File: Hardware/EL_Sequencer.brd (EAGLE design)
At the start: 57.1 x 82.5 mm, 106 parts, among them J1 Battery, J2 DC-OUTPUT, J3 AC-INPUT, U1 LM317, U10 Z0103MN, U11 Z0103MN, U12 Z0103MN, U13 MOC3063S, U14 MOC3063S, U15 MOC3063S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

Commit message: Version 2.1 hardware files
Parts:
- added U$9: REVISION, SparkFun-Aesthetics:REVISION
- C1, C4, C5, C6, C7: device SparkFun:0402-CAP -> SparkFun-Capacitors:0603-CAP
- C2, C3: device SparkFun:EIA3216 -> SparkFun-Capacitors:EIA3216
- R1, R14, R15, R16, R17, R18, R19, R2, R20, R21, R26, R27, R28, R29, R30, R31, R32, R33: device SparkFun:0603-RES -> SparkFun-Resistors:0603-RES
- R10, R11, R12, R13, R22, R23, R24, R25, R3, R4, R5, R6, R7, R8, R9: device SparkFun:0402-RES -> SparkFun-Resistors:0603-RES
- moved FRAME1 19.1 mm to (5.08, -14.0)
- moved FRAME2 19.1 mm to (5.08, -14.0)
- moved R4 4.49 mm to (50.2, 4.45), turned to 180 degrees
- moved R6 3.18 mm to (20.3, 34.9), turned to 270 degrees
- moved R13 2.54 mm to (20.3, 38.1), turned to 270 degrees
- moved C5 1.91 mm to (17.8, 32.4), turned to 180 degrees
- moved R11 1.91 mm to (20.3, 20.3), turned to 270 degrees
- moved R5 1.91 mm to (21.6, 32.4), turned to 0 degrees
- moved C6 0.71 mm to (5.08, 17.5)
- moved C4 0.64 mm to (18.7, 17.4)
- moved R3 0.64 mm to (39.4, 4.45)
- turned R8 to 180 degrees
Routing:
- net GND: track 116.4 -> 122.3 mm
- net RXI: track 56.8 -> 61.1 mm
- net RST: track 40.7 -> 43.5 mm
- net FTDI_DTR: track 42.1 -> 39.6 mm
- net DTR: track 12.7 -> 14.9 mm
- net VCC: track 154.0 -> 156.1 mm
- net ADC_7*: track 6.95 -> 8.51 mm
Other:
- board text added: "Nathan Seidle, Mike Grusin"
- board text added: "Toni Klopfenstein"

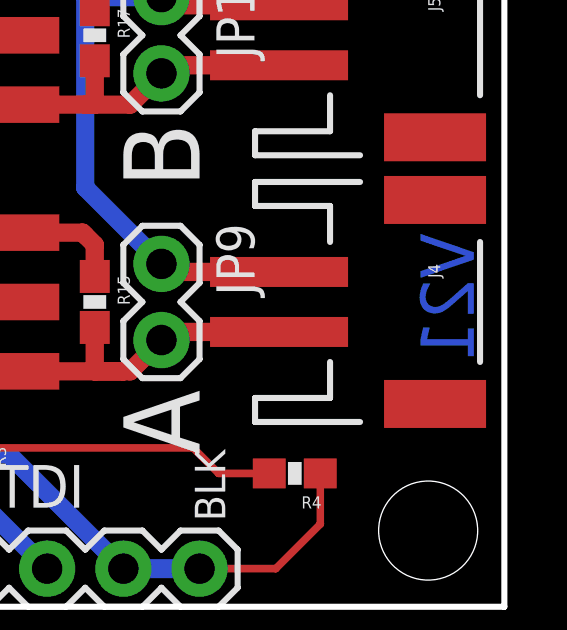
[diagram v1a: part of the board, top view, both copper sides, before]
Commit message: Fixing versions to 2.2
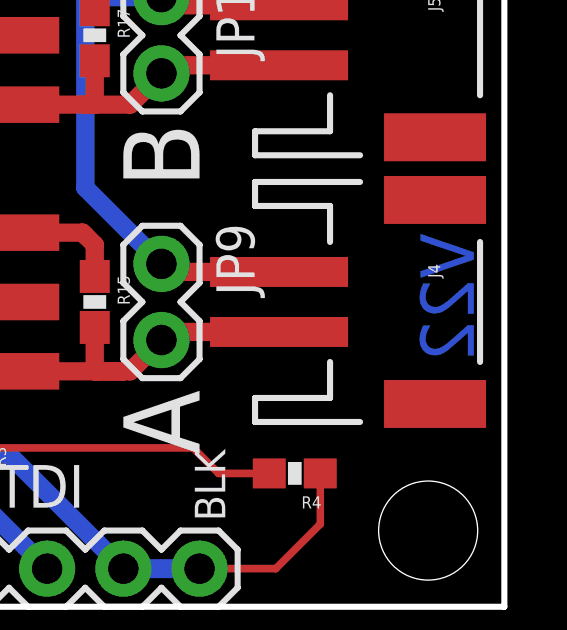
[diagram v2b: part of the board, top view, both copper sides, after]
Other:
- board text added: "V22"
- board text removed: "V21"
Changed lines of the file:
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@@
 <text x="5.969" y="48.006" size="1.4224" layer="21" font="vector" ratio="15" rot="SR270">BATT</text>
 <text x="15.494" y="47.498" size="1.4224" layer="21" font="vector" ratio="15" rot="SR270">USB</text>
-<text x="56.134" y="12.446" size="1.778" layer="16" font="vector" ratio="20" rot="SMR270">V21</text>
+<text x="56.134" y="12.446" size="1.778" layer="16" font="vector" ratio="20" rot="SMR270">V22</text>
 <text x="46.99" y="58.42" size="2.54" layer="21" font="vector" ratio="15" rot="R90">G</text>
 <text x="46.99" y="67.31" size="2.54" layer="21" font="vector" ratio="15" rot="R90">H</text>
